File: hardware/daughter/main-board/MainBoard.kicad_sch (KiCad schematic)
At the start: 30 parts, among them U1 ADG1414BRUZ, U10 CD22M3494MQZ, U11 CD22M3494MQZ, U12 CD22M3494MQZ, U13 ADG1414BRUZ, U14 ADG1414BRUZ, U2 ADG1414BRUZ, U3 ADG1414BRUZ, U4 ADG1414BRUZ, U5 TL071, U6 TL071, U7 TL071, U8 TL071, U9 CD22M3494MQZ

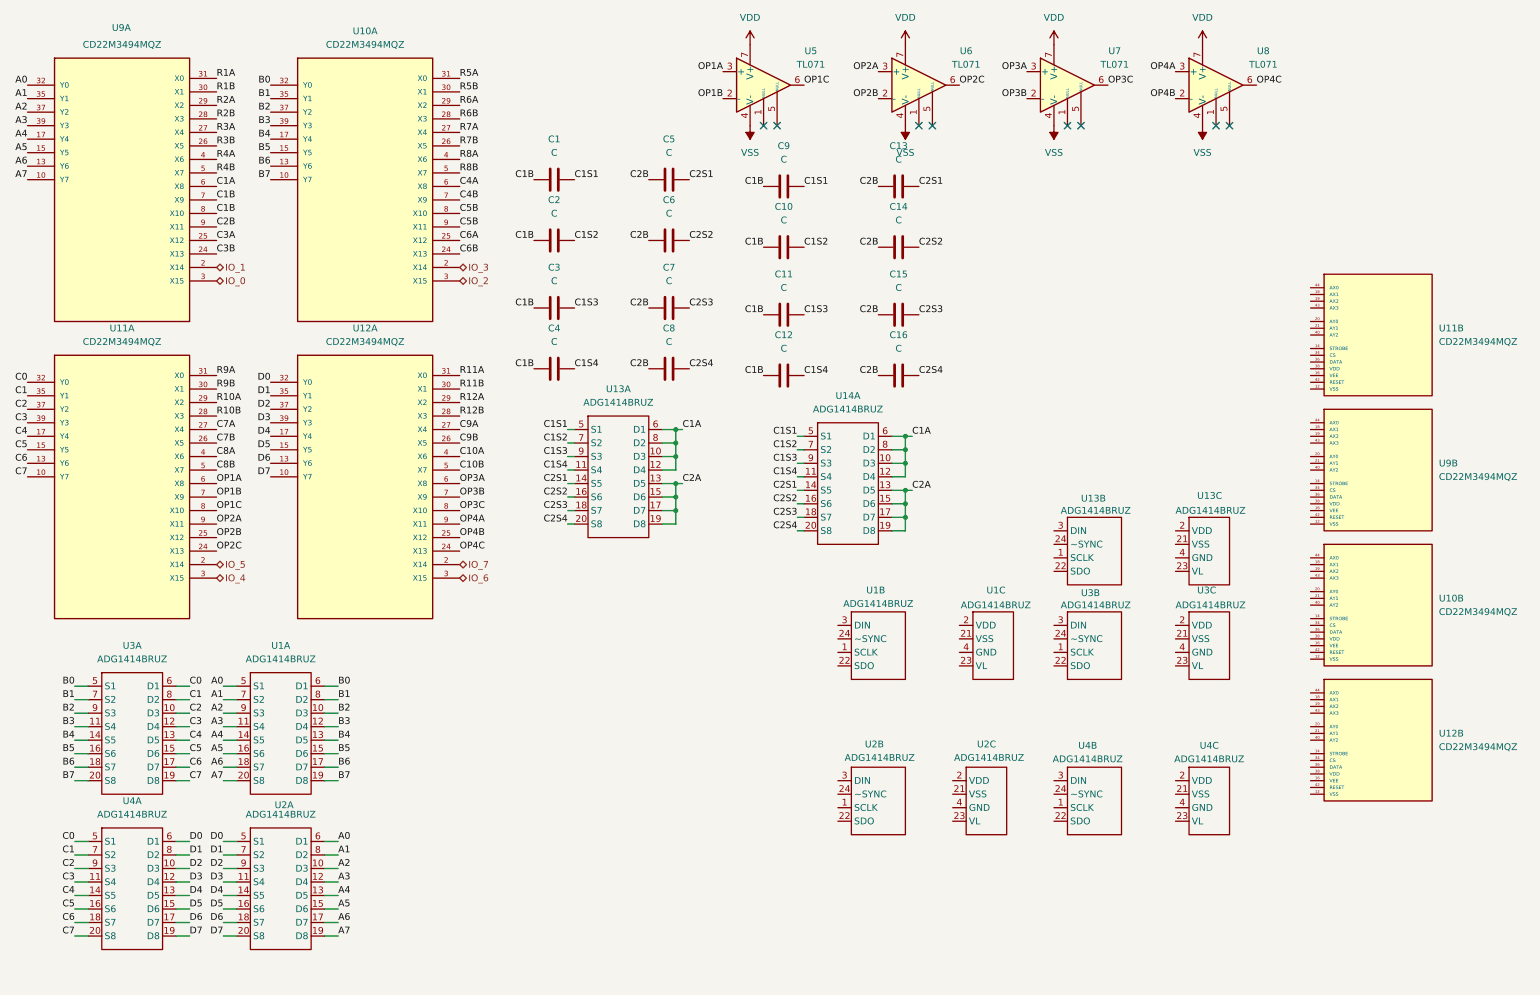
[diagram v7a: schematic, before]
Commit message: staged into root heirachical sheets, moved cell arch into cells sheet
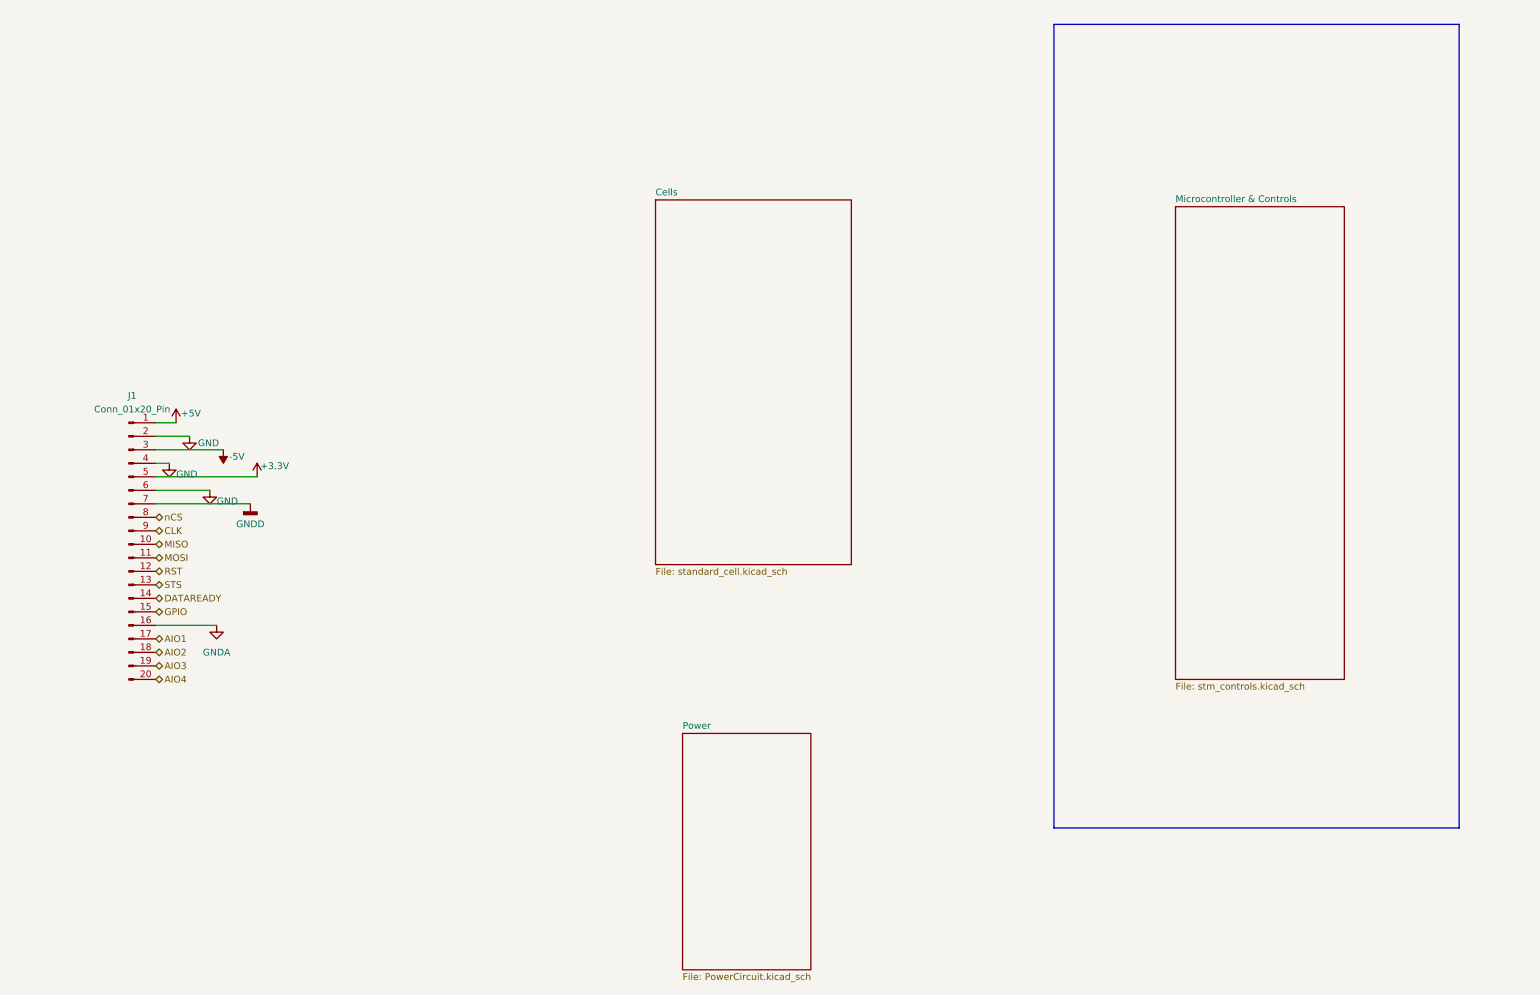
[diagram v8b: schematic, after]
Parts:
- removed C1, C10, C11, C12, C13, C14, C15, C16, C2, C3, C4, C5, C6, C7, C8, C9: C, symbol Device:C
- removed U1, U13, U14, U2, U3, U4: ADG1414BRUZ, symbol SeniorDesign:ADG1414BRU_1
- removed U10, U11, U12, U9: CD22M3494MQZ, MT8816AF1:QFP80P1200X1200X120-44N, symbol SeniorDesign:CD22M3494MQZ
- removed U5, U6, U7, U8: TL071, symbol Amplifier_Operational:TL071
- added J1: Conn_01x20_Pin, symbol Connector:Conn_01x20_Pin
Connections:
- new net +3.3V: J1.5 (Pin_5)
- new net +5V: J1.1 (Pin_1)
- new net -5V: J1.3 (Pin_3)
- new net AIO1: J1.17 (Pin_17)
- new net AIO2: J1.18 (Pin_18)
- new net AIO3: J1.19 (Pin_19)
- new net AIO4: J1.20 (Pin_20)
- new net CLK: J1.9 (Pin_9)
- new net DATAREADY: J1.14 (Pin_14)
- new net GND: J1.2 (Pin_2), J1.4 (Pin_4), J1.6 (Pin_6)
- new net GNDA: J1.16 (Pin_16)
- new net GNDD: J1.7 (Pin_7)
- new net GPIO: J1.15 (Pin_15)
- new net MISO: J1.10 (Pin_10)
- new net MOSI: J1.11 (Pin_11)
- new net RST: J1.12 (Pin_12)
- new net STS: J1.13 (Pin_13)
- new net nCS: J1.8 (Pin_8)
- no-connect marks 8 -> 0
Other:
- added sheet Cells (standard_cell.kicad_sch)
- added sheet Microcontroller & Controls (stm_controls.kicad_sch)
- added sheet Power (PowerCircuit.kicad_sch)
